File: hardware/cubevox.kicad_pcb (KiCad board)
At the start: 4 copper layers, 200 x 150 mm, 223 parts, among them J1 USB-C, J101 J_IN NCJ6FA-H, J106 DC 9V, J108 OUT 6.35mm, J117 OLED SH1106, J3 TC2030-NL SWD, K101 G6K-2F-Y DC5, K102 G6K-2F-Y DC5, Q101 MMBT3904, SW101 ST-0-102 bat toggle, SW102 ST-0-102 bat toggle, SW103 ST-0-102 bat toggle, SW104 ST-0-102 bat toggle, SW105 ST-0-102 bat toggle, SW106 ST-0-102 bat toggle, SW107 ST-0-102 bat toggle, SW108 ST-0-102 bat toggle, U1 STM32H743VIT6, U101 CD74HC4067, U103 AP63205WU-7, U104 OPA2197IDR, U105 OPA2197IDR, U106 OPA2197IDR, U3 AP63203WU-7, U4 TLV75533PDBVR, U6 PCM5102APWR, U8 PCM1808PWR, Y1 25MHz 12pF

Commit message: layout: change on /3V3,/GND (ledger 0098)
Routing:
- net /3V3: track 610.6 -> 639.1 mm

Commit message: layout: change on /3V3 (ledger 0099)
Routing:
- net /3V3: track 639.1 -> 637.6 mm

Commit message: layout: change on /3V3 (ledger 0100)
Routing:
- net /3V3: track 637.6 -> 638.5 mm
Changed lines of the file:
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@@
+	)
+	(segment
+		(start 93.8 99.85)
+		(end 77.35 99.85)
+		(width 0.4)
+		(layer "In2.Cu")
+		(net "/3V3")
 	)
 	(segment
@@
 	)
 	(segment
-		(start 92.5 98.55)
-		(end 76.05 98.55)
-		(width 0.4)
-		(layer "In2.Cu")
-		(net "/3V3")
-	)
-	(segment
 		(start 124.7 101.95)
 		(end 125.25 102.5)
@@
 	)
 	(segment
-		(start 93.15 99.2)
-		(end 92.5 98.55)
+		(start 207.6 123.8)
+		(end 231.6 123.8)
 		(width 0.4)
 		(layer "In2.Cu")
@@
 	)
 	(segment
-		(start 207.6 123.8)
-		(end 231.6 123.8)
-		(width 0.4)
-		(layer "In2.Cu")
-		(net "/3V3")
-	)
-	(segment
 		(start 169.05 65.15)
 		(end 170 66.099999)
@@
 	)
 	(segment
+		(start 77.35 99.85)
+		(end 76.05 98.55)
+		(width 0.4)
+		(layer "In2.Cu")
+		(net "/3V3")
+	)
+	(segment
 		(start 112.15 62.75)
 		(end 117.25 62.75)
@@
 	)
 	(segment
+		(start 92.4 93.35)
+		(end 93.15 94.1)
+		(width 0.4)
+		(layer "In2.Cu")
+		(net "/3V3")
+	)
+	(segment
 		(start 83.5 79.4)
 		(end 82.55 80.35)
@@
 		(width 0.4)
 		(layer "In2.Cu")
-		(net "/3V3")
-	)
-	(segment
-		(start 92.4 93.35)
-		(end 93.15 94.1)
-		(width 0.4)
-		(layer "In2.Cu")

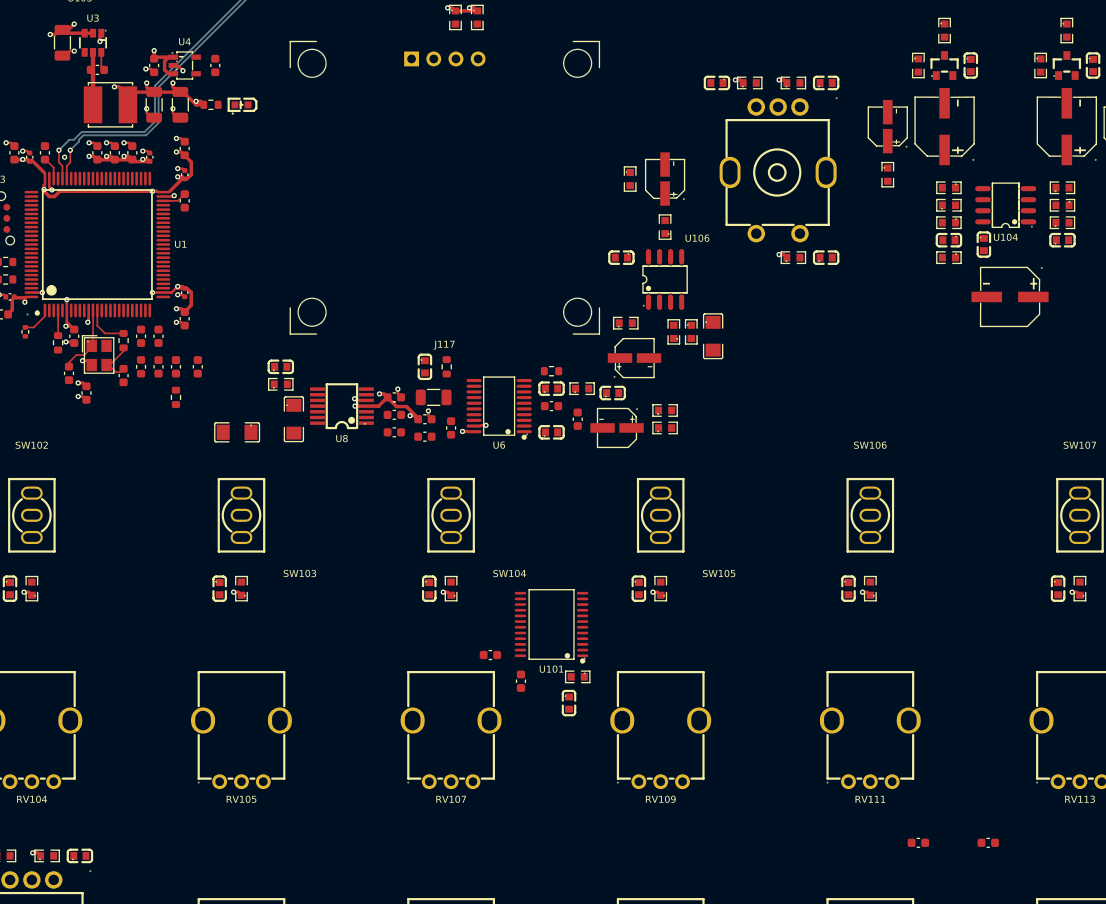
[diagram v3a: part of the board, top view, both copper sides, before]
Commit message: layout: change on /3V3A,/GND (ledger 0101)
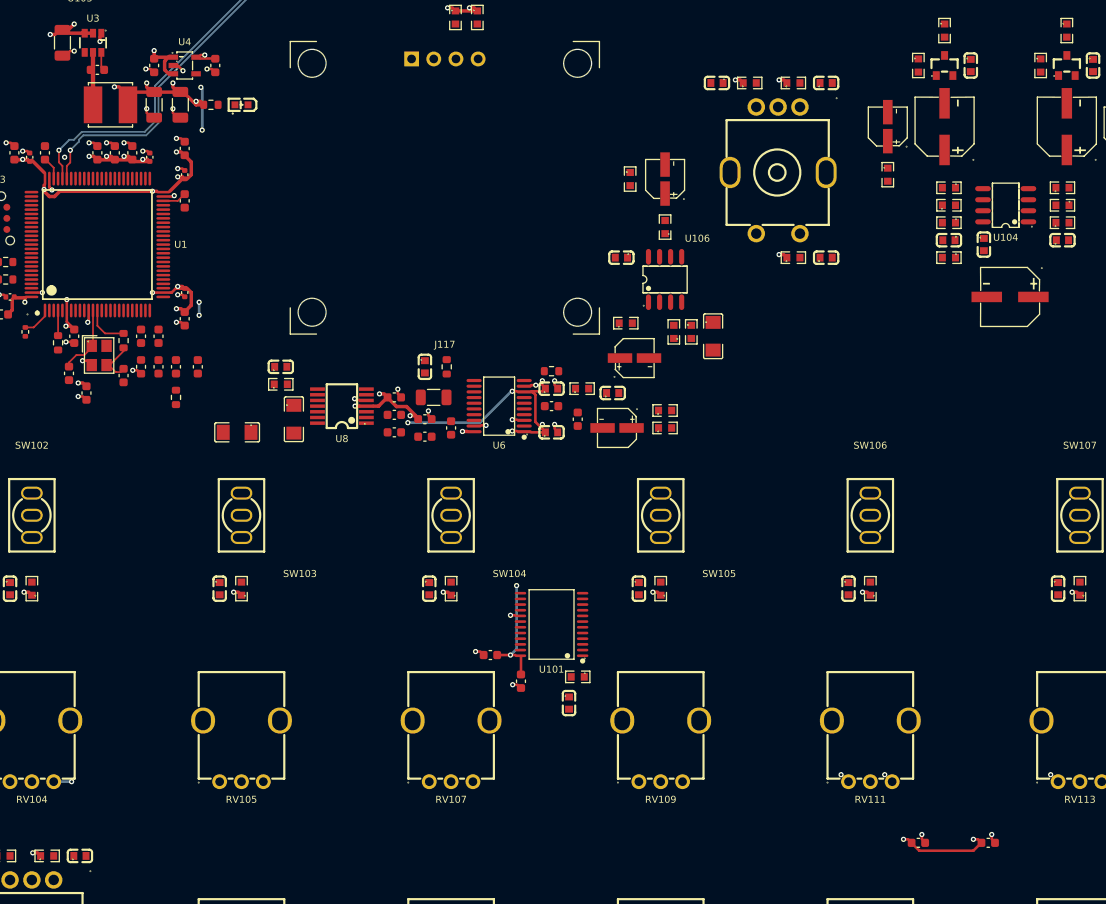
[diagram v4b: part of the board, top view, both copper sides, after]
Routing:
- net /3V3A: track 0.00 -> 498.8 mm, vias 0 -> 17
- net /GND: track 18.4 -> 23.9 mm, vias 35 -> 47

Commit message: layout: change on /5VA,/GND (ledger 0102)
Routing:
- net /5VA: track 0.00 -> 231.6 mm, vias 0 -> 14
- net /GND: track 23.9 -> 28.5 mm, vias 47 -> 56

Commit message: layout: change on /9V_JACK (ledger 0103)
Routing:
- net /9V_JACK: track 0.00 -> 18.7 mm, vias 0 -> 2
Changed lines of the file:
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@@
+	)
+	(segment
+		(start 233.6 35.25)
+		(end 233.55 35.25)
+		(width 0.4)
+		(layer "F.Cu")
+		(net "/9V_JACK")
+	)
+	(segment
+		(start 233.5 47.75)
+		(end 233.5 48.25)
+		(width 0.4)
+		(layer "F.Cu")
+		(net "/9V_JACK")
+	)
+	(via
+		(at 233.5 48.25)
+		(size 0.6)
+		(drill 0.3)
+		(layers "F.Cu" "B.Cu")
+		(net "/9V_JACK")
+	)
+	(via
+		(at 233.55 35.25)
+		(size 0.6)
+		(drill 0.3)
+		(layers "F.Cu" "B.Cu")
+		(net "/9V_JACK")
+	)
+	(segment
+		(start 234.35 47.4)
+		(end 234.35 37)
+		(width 0.4)
+		(layer "In2.Cu")
+		(net "/9V_JACK")
+	)
+	(segment
+		(start 233.55 36.2)
+		(end 233.55 35.25)
+		(width 0.4)
+		(layer "In2.Cu")
+		(net "/9V_JACK")
+	)
+	(segment
+		(start 234.35 37)
+		(end 233.55 36.2)
+		(width 0.4)
+		(layer "In2.Cu")
+		(net "/9V_JACK")
+	)
+	(segment
+		(start 233.55 35.25)
+		(end 232.3 34)
+		(width 0.4)
+		(layer "In2.Cu")
+		(net "/9V_JACK")
+	)
+	(segment
+		(start 233.5 48.25)
+		(end 234.35 47.4)
+		(width 0.4)
+		(layer "In2.Cu")
+		(net "/9V_JACK")
+	)
+	(segment
+		(start 232.3 34)
+		(end 229.65 34)
+		(width 0.4)
+		(layer "In2.Cu")
+		(net "/9V_JACK")
 	)
 	(segment

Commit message: layout: change on /GND,/VIN_9V (ledger 0104)
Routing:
- net /VIN_9V: track 0.00 -> 154.6 mm, vias 0 -> 7
- net /GND: track 28.5 -> 30.1 mm, vias 56 -> 60

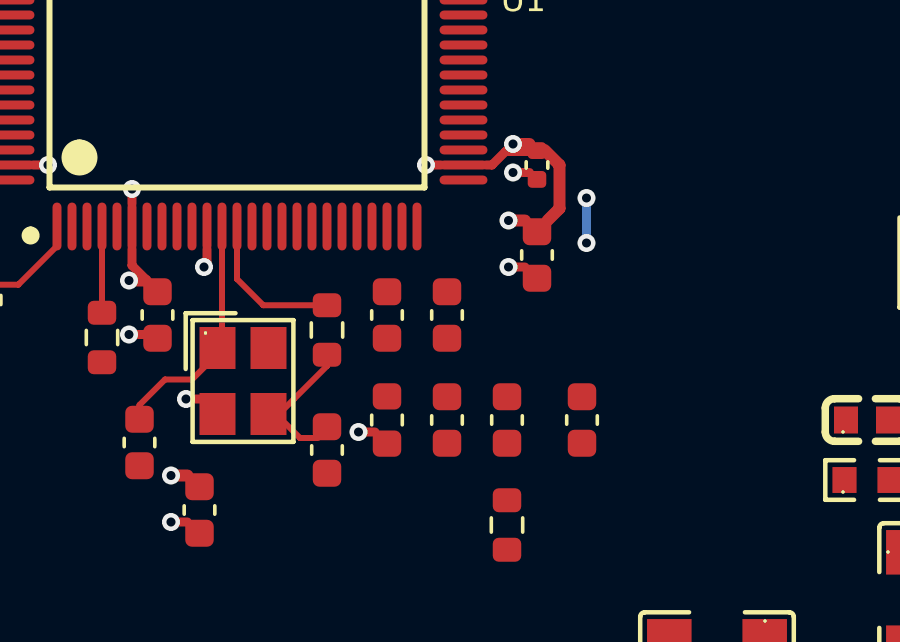
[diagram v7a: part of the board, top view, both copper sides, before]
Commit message: layout: change on /GND,/h7core_block/VDDA (ledger 0105)
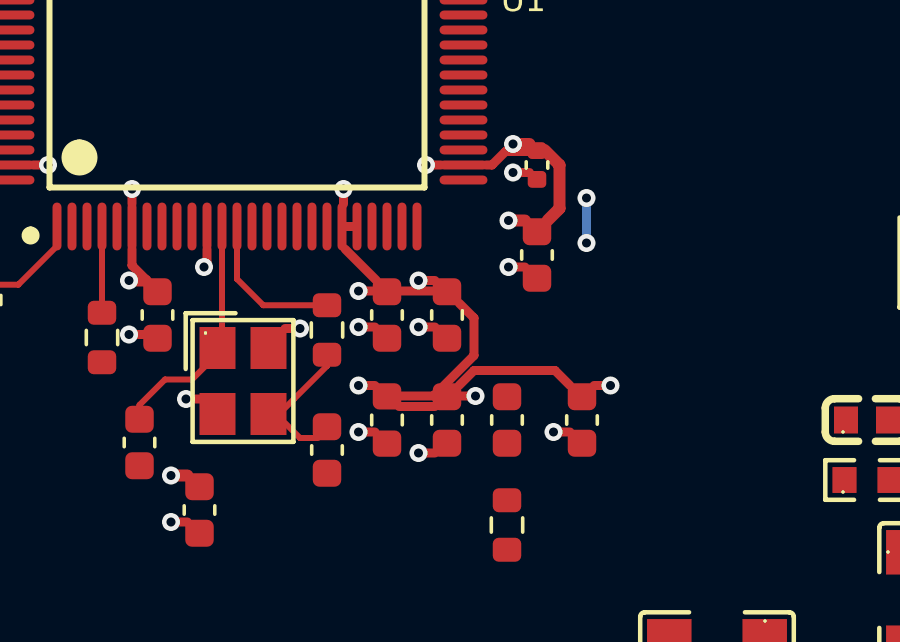
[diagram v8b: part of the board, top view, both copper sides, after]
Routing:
- net /h7core_block/VDDA: track 0.00 -> 30.1 mm, vias 0 -> 6
- net /GND: track 30.1 -> 32.8 mm, vias 60 -> 65
